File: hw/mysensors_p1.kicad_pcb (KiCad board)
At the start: 2 copper layers, 58.4 x 73.7 mm, 8 parts, among them J1 RJ12, J2 Conn_01x06_Socket, U2 NRF24L01_Breakout

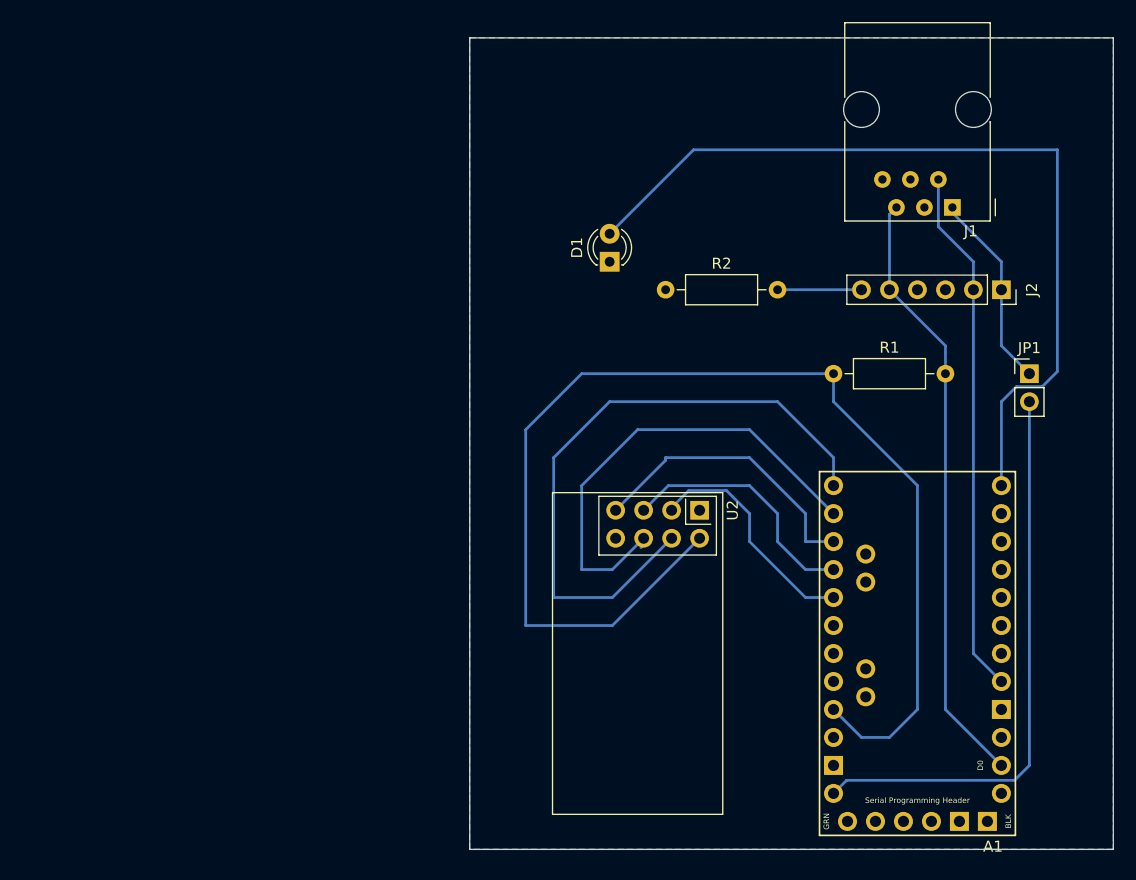
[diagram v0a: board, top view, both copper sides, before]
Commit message: More or less working, just electricity power for now.
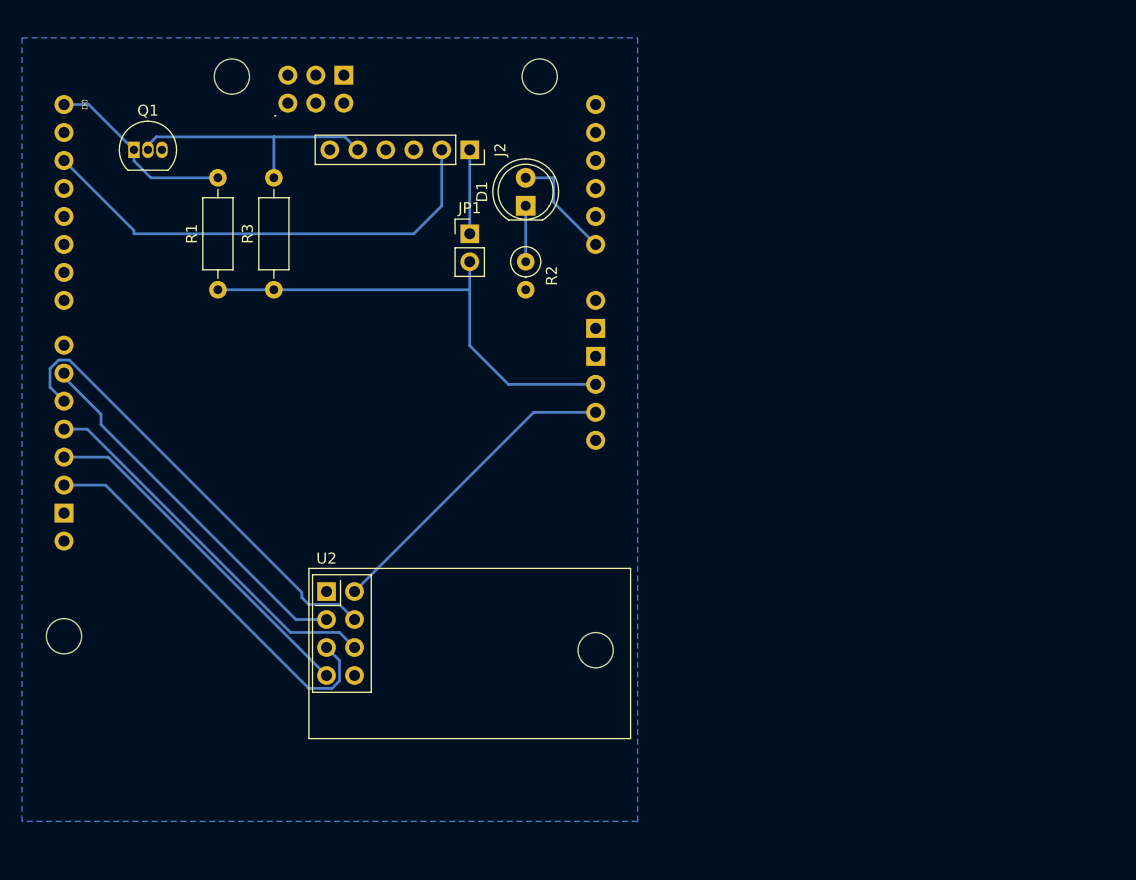
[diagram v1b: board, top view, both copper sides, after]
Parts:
- removed J1: RJ12, Connector_RJ:RJ12_Amphenol_54601
- added Q1: BS170, Package_TO_SOT_THT:TO-92_Inline, F.Cu at (73.7, 63.5)
- added R3: 4k7, Resistor_THT:R_Axial_DIN0207_L6.3mm_D2.5mm_P10.16mm_Horizontal, F.Cu at (86.4, 76.2)
- A1: value Arduino_Pro_Mini_Socket -> Arduino_Uno_R2_Shield; footprint PCM_arduino-library:Arduino_Pro_Mini_Socket -> PCM_arduino-library:Arduino_Uno_R2_Shield
- D1: footprint LED_THT:LED_D3.0mm -> LED_THT:LED_D5.0mm
- R2: footprint Resistor_THT:R_Axial_DIN0207_L6.3mm_D2.5mm_P10.16mm_Horizontal -> Resistor_THT:R_Axial_DIN0207_L6.3mm_D2.5mm_P2.54mm_Vertical
- moved R1 56.4 mm to (81.3, 76.2), turned to 90 degrees
- moved JP1 52.4 mm to (104.1, 71.1)
- moved J2 49.9 mm to (104.1, 63.5)
- moved U2 34.7 mm to (91.1, 103.6), turned to 0 degrees
- moved A1 30.0 mm to (118.1, 122.9), turned to 90 degrees
- moved R2 13.0 mm to (109.2, 73.7), turned to -90 degrees
- moved D1 9.16 mm to (109.2, 68.6)
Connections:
- A1 pad A0: CE -> LED
- A1 pad D0: TX -> TX inverted
- A1 pad D9: LED -> CE
- A1 pad GND1: unconnected-(A1-GND-PadGND1) -> GND
- R1 pad 1: +3V3 -> +5V
- R1 pad 2: TX -> TX inverted
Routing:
- net +3V3: track 110.3 -> 28.6 mm
- net LED: track 77.8 -> 10.2 mm
- net TX: track 56.2 -> 24.0 mm
- net TX inverted: track 0.00 -> 17.3 mm
- net CS: track 57.8 -> 41.5 mm
- net SCK: track 22.8 -> 36.4 mm
- net CE: track 21.1 -> 33.9 mm
- net Net-(J2-Pin_1): track 18.0 -> 7.62 mm
- net MOSI: track 43.3 -> 34.6 mm
- net +5V: track 51.9 -> 43.4 mm
- net GND: track 7.62 -> 0.00 mm
- net MISO: track 26.5 -> 32.0 mm
- net Net-(D1-K): track 0.00 -> 5.08 mm
- net DTR: track 47.9 -> 43.4 mm
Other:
- board outline removed
